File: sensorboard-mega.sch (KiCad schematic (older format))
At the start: 19 parts, among them P1 Digital, P10 CONN_01X01, P11 CONN_01X01, P12 CONN_01X01, P13 CONN_01X01, P2 Power, P3 Analog, P4 Analog, P5 PWM, P6 PWM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

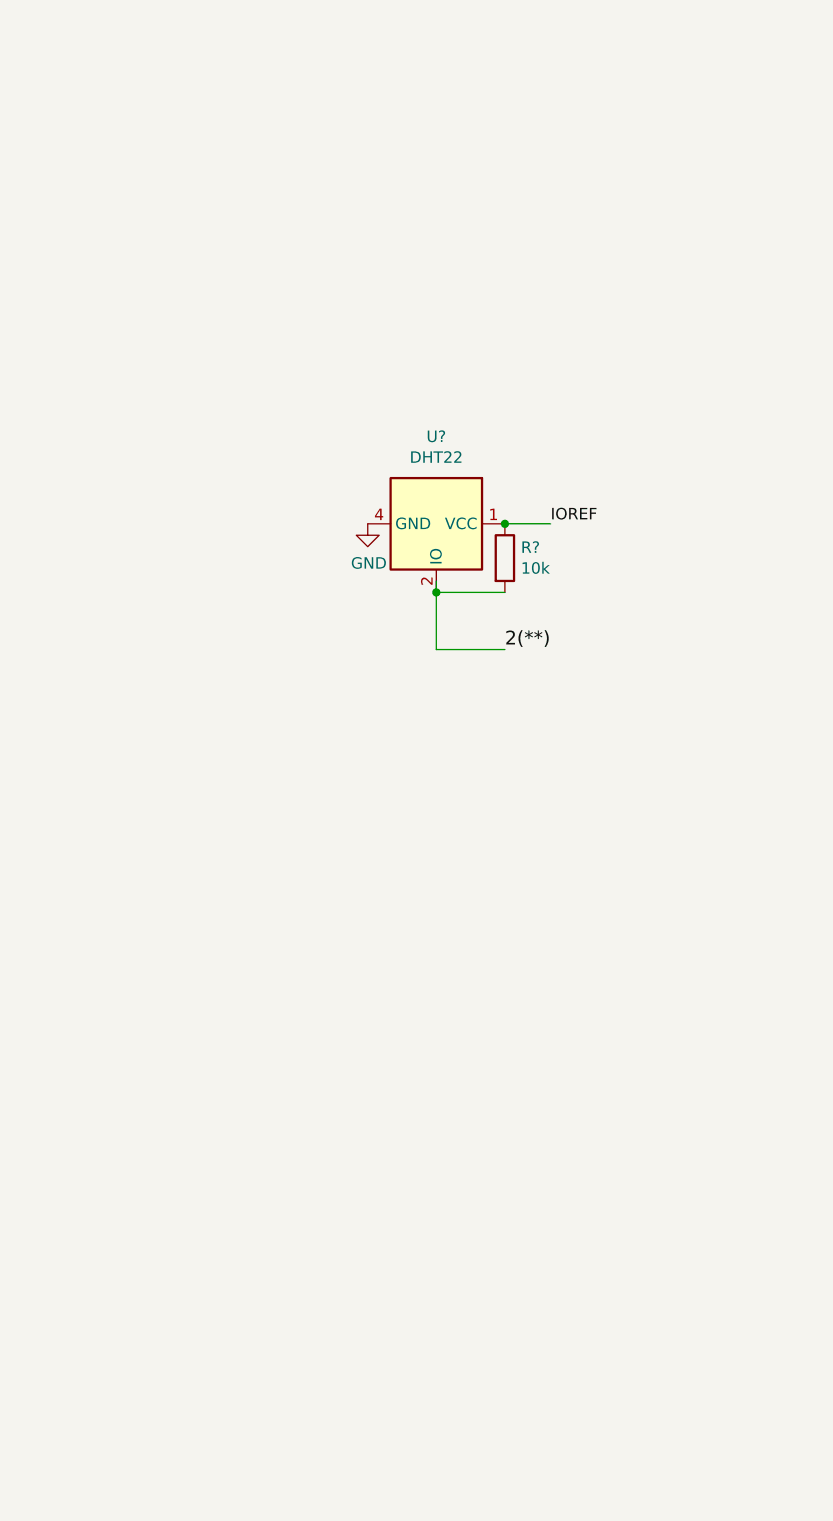
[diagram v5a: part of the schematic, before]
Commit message: Add all onboard sensors
The sensors are:
Barometer sensor
DHT22 sensor
DS3231 RTC
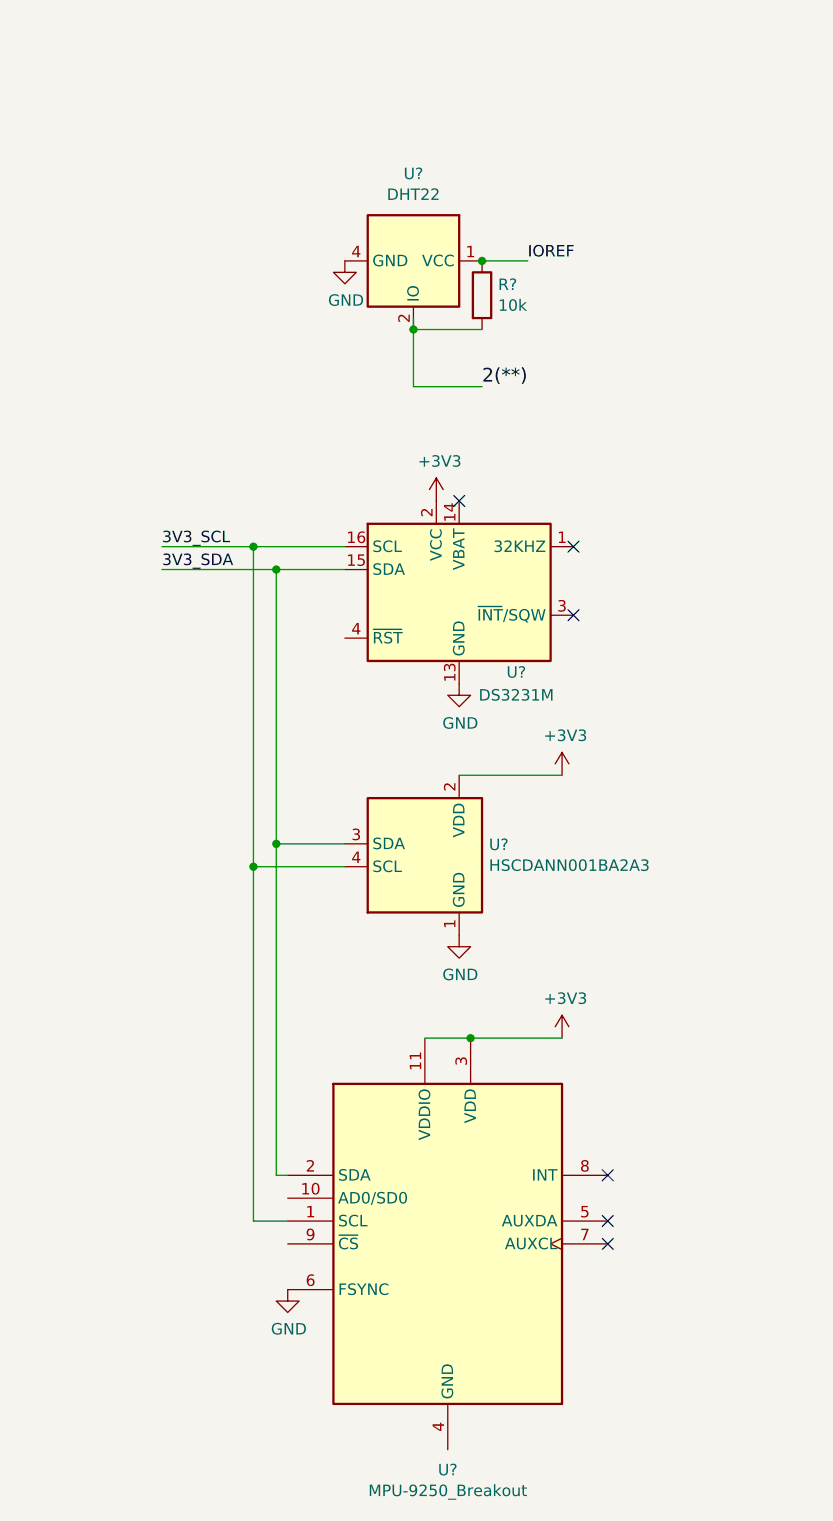
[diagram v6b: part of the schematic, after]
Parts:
- added U?: DS3231M, Package_SO:SOIC-16W_7.5x10.3mm_P1.27mm, symbol Timer_RTC:DS3231M
- added U?: HSCDANN001BA2A3, Package_DIP:DIP-8_W7.62mm, symbol New_Library:HSCDANN001BA2A3
- added U?: MPU-9250_Breakout, Sensor_Motion:InvenSense_QFN-24_3x3mm_P0.4mm, symbol New_Library:MPU-9250_Breakout
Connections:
- net +3V3: now also U?.11 (VDDIO), U?.2 (VCC), U?.2 (VDD), U?.3 (VDD)
- net 3V3_SCL: now also U?.1 (SCL), U?.16 (SCL), U?.4 (SCL)
- net 3V3_SDA: now also U?.15 (SDA), U?.2 (SDA), U?.3 (SDA)
- net GND: now also U?.1 (GND), U?.10 (GND), U?.11 (GND), U?.12 (GND), U?.13 (GND), U?.5 (GND), U?.6 (FSYNC), U?.6 (GND), U?.7 (GND), U?.8 (GND), U?.9 (GND)
- no-connect marks 7 -> 13
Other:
- moved on the sheet: R?, U?
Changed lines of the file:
@@
 $EndComp
 Wire Wire Line
-	5850 3050 6050 3050
-Text Label 6050 3050 0    50   ~ 0
+	5750 1900 5950 1900
+Text Label 5950 1900 0    50   ~ 0
 IOREF
 $Comp
 L Device:R R?
 U 1 1 5DF91E75
-P 5850 3200
-F 0 "R?" H 5920 3246 50  0000 L CNN
-F 1 "10k" H 5920 3155 50  0000 L CNN
-F 2 "" V 5780 3200 50  0001 C CNN
-F 3 "~" H 5850 3200 50  0001 C CNN
-	1    5850 3200
-	1    0    0    -1
-$EndComp
-Wire Wire Line
-	5850 3350 5550 3350
+P 5750 2050
+F 0 "R?" H 5820 2096 50  0000 L CNN
+F 1 "10k" H 5820 2005 50  0000 L CNN
+F 2 "" V 5680 2050 50  0001 C CNN
+F 3 "~" H 5750 2050 50  0001 C CNN
+	1    5750 2050
+	1    0    0    -1
+$EndComp
+Wire Wire Line
+	5750 2200 5450 2200
 $Comp
 L power:GND #PWR?
 U 1 1 5DF988E0
-P 5250 3050
-F 0 "#PWR?" H 5250 2800 50  0001 C CNN
-F 1 "GND" H 5255 2877 50  0000 C CNN
-F 2 "" H 5250 3050 50  0001 C CNN
-F 3 "" H 5250 3050 50  0001 C CNN
-	1    5250 3050
+P 5150 1900
+F 0 "#PWR?" H 5150 1650 50  0001 C CNN
+F 1 "GND" H 5155 1727 50  0000 C CNN
+F 2 "" H 5150 1900 50  0001 C CNN
+F 3 "" H 5150 1900 50  0001 C CNN
+	1    5150 1900
 	1    0    0    -1
 $EndComp
@@
 L Sensor:DHT22 U?
 U 1 1 5DF9B2BC
-P 5550 3050
-F 0 "U?" V 5169 3050 50  0000 C CNN
-F 1 "DHT22" V 5260 3050 50  0000 C CNN
-F 2 "Sensor:Aosong_DHT11_5.5x12.0_P2.54mm" H 5550 2650 50  0001 C CNN
-F 3 "http://akizukidenshi.com/download/ds/aosong/DHT11.pdf" H 5700 3300 50  0001 C CNN
-	1    5550 3050
+P 5450 1900
+F 0 "U?" V 5069 1900 50  0000 C CNN
+F 1 "DHT22" V 5160 1900 50  0000 C CNN
+F 2 "Sensor:Aosong_DHT11_5.5x12.0_P2.54mm" H 5450 1500 50  0001 C CNN
+F 3 "http://akizukidenshi.com/download/ds/aosong/DHT11.pdf" H 5600 2150 50  0001 C CNN
+	1    5450 1900
 	0    1    1    0
 $EndComp
-Connection ~ 5850 3050
+Connection ~ 5750 1900
 Text Notes 700  5500 0    50   ~ 0
 Note: Bridge the HV and LV signal pins using wire for Arduino Due
 Wire Wire Line
-	5550 3300 5550 3350
-Connection ~ 5550 3350
-Wire Wire Line
-	5550 3350 5550 3600
-Wire Wire Line
-	5550 3600 5850 3600
-Text Label 5850 3600 0    60   ~ 0
+	5450 2150 5450 2200
+Connection ~ 5450 2200
+Wire Wire Line
+	5450 2200 5450 2450
+Wire Wire Line
+	5450 2450 5750 2450
+Text Label 5750 2450 0    60   ~ 0
 2(**)
 $Comp
@@
 Text Label 800  6500 0    50   ~ 0
 3v3_SS
+$Comp
+L Timer_RTC:DS3231M U?
+U 1 1 5DEAA5E1
+P 5650 3350
+F 0 "U?" H 5900 3000 50  0000 C CNN
+F 1 "DS3231M" H 5900 2900 50  0000 C CNN
+F 2 "Package_SO:SOIC-16W_7.5x10.3mm_P1.27mm" H 5650 2750 50  0001 C CNN
+F 3 "http://datasheets.maximintegrated.com/en/ds/DS3231.pdf" H 5920 3400 50  0001 C CNN
+	1    5650 3350
+	1    0    0    -1
+$EndComp
+$Comp
+L New_Library:HSCDANN001BA2A3 U?
+U 1 1 5DEAAED6
+P 5550 4550
+F 0 "U?" H 5780 4646 50  0000 L CNN
+F 1 "HSCDANN001BA2A3" H 5780 4555 50  0000 L CNN
+F 2 "Package_DIP:DIP-8_W7.62mm" H 5550 3850 50  0001 C CNN
+F 3 "https://sensing.honeywell.com/honeywell-sensing-trustability-hsc-series-high-accurboard-mount-pressure-sensors-50099148-a-en.pdf" H 5550 4550 50  0001 C CNN
+	1    5550 4550
+	1    0    0    -1
+$EndComp
+$Comp
+L New_Library:MPU-9250_Breakout U?
+U 1 1 5DEAC0F0
+P 5600 6200
+F 0 "U?" H 5600 5211 50  0000 C CNN
+F 1 "MPU-9250_Breakout" H 5600 5120 50  0000 C CNN
+F 2 "Sensor_Motion:InvenSense_QFN-24_3x3mm_P0.4mm" H 5600 5200 50  0001 C CNN
+F 3 "https://store.invensense.com/datasheets/invensense/MPU9250REV1.0.pdf" H 5600 6050 50  0001 C CNN
+	1    5600 6200
+	1    0    0    -1
+$EndComp
+Wire Wire Line
+	5150 3150 4750 3150
+Wire Wire Line
+	4750 3150 4750 4550
+Wire Wire Line
+	5150 4550 4750 4550
+Connection ~ 4750 4550
+Wire Wire Line
+	4850 3250 5150 3250
+Wire Wire Line
+	5150 4450 4850 4450
+Connection ~ 4850 4450
+Wire Wire Line
+	4850 4450 4850 3250
+Wire Wire Line
+	4750 3150 4350 3150
+Connection ~ 4750 3150
+Wire Wire Line
+	4850 3250 4350 3250
+Connection ~ 4850 3250
+Text Label 4350 3250 0    50   ~ 0
+3V3_SDA
+Text Label 4350 3150 0    50   ~ 0
+3V3_SCL
+NoConn ~ 5650 2950
+NoConn ~ 6150 3150
+NoConn ~ 6150 3450
+NoConn ~ 6300 6100
+NoConn ~ 6300 6200
+NoConn ~ 6300 5900
+$Comp
+L power:GND #PWR?
+U 1 1 5DF6484B
+P 4900 6400
+F 0 "#PWR?" H 4900 6150 50  0001 C CNN
+F 1 "GND" H 4905 6227 50  0000 C CNN
+F 2 "" H 4900 6400 50  0001 C CNN
+F 3 "" H 4900 6400 50  0001 C CNN
+	1    4900 6400
+	1    0    0    -1
+$EndComp
+$Comp
+L power:GND #PWR?
+U 1 1 5DF67973
+P 5650 4850
+F 0 "#PWR?" H 5650 4600 50  0001 C CNN
+F 1 "GND" H 5655 4677 50  0000 C CNN
+F 2 "" H 5650 4850 50  0001 C CNN
+F 3 "" H 5650 4850 50  0001 C CNN
+	1    5650 4850
+	1    0    0    -1
+$EndComp
+Wire Wire Line
+	4900 6100 4750 6100
+Wire Wire Line
+	4750 4550 4750 6100
+Wire Wire Line
+	4900 5900 4850 5900
+Wire Wire Line
+	4850 4450 4850 5900
+Wire Wire Line
+	5500 5300 5700 5300
+Wire Wire Line
+	5700 5300 6100 5300
+Connection ~ 5700 5300
+$Comp
+L power:+3V3 #PWR?
+U 1 1 5DFA056E
+P 6100 5300
+F 0 "#PWR?" H 6100 5150 50  0001 C CNN
+F 1 "+3V3" H 6115 5473 50  0000 C CNN
+F 2 "" H 6100 5300 50  0001 C CNN
+F 3 "" H 6100 5300 50  0001 C CNN
+	1    6100 5300
+	1    0    0    -1
+$EndComp
+Wire Wire Line
+	5650 4150 6100 4150
+$Comp
+L power:+3V3 #PWR?
+U 1 1 5DFA9209
+P 6100 4150
+F 0 "#PWR?" H 6100 4000 50  0001 C CNN
+F 1 "+3V3" H 6115 4323 50  0000 C CNN
+F 2 "" H 6100 4150 50  0001 C CNN
+F 3 "" H 6100 4150 50  0001 C CNN
+	1    6100 4150
+	1    0    0    -1
+$EndComp
+$Comp
+L power:GND #PWR?
+U 1 1 5DFAA3A6
+P 5650 3750
+F 0 "#PWR?" H 5650 3500 50  0001 C CNN
+F 1 "GND" H 5655 3577 50  0000 C CNN
+F 2 "" H 5650 3750 50  0001 C CNN
+F 3 "" H 5650 3750 50  0001 C CNN
+	1    5650 3750
+	1    0    0    -1
+$EndComp
+$Comp
+L power:+3V3 #PWR?
+U 1 1 5DFAFB69
+P 5550 2950
+F 0 "#PWR?" H 5550 2800 50  0001 C CNN
+F 1 "+3V3" H 5565 3123 50  0000 C CNN
+F 2 "" H 5550 2950 50  0001 C CNN
+F 3 "" H 5550 2950 50  0001 C CNN
+	1    5550 2950
+	1    0    0    -1
+$EndComp
 $EndSCHEMATC

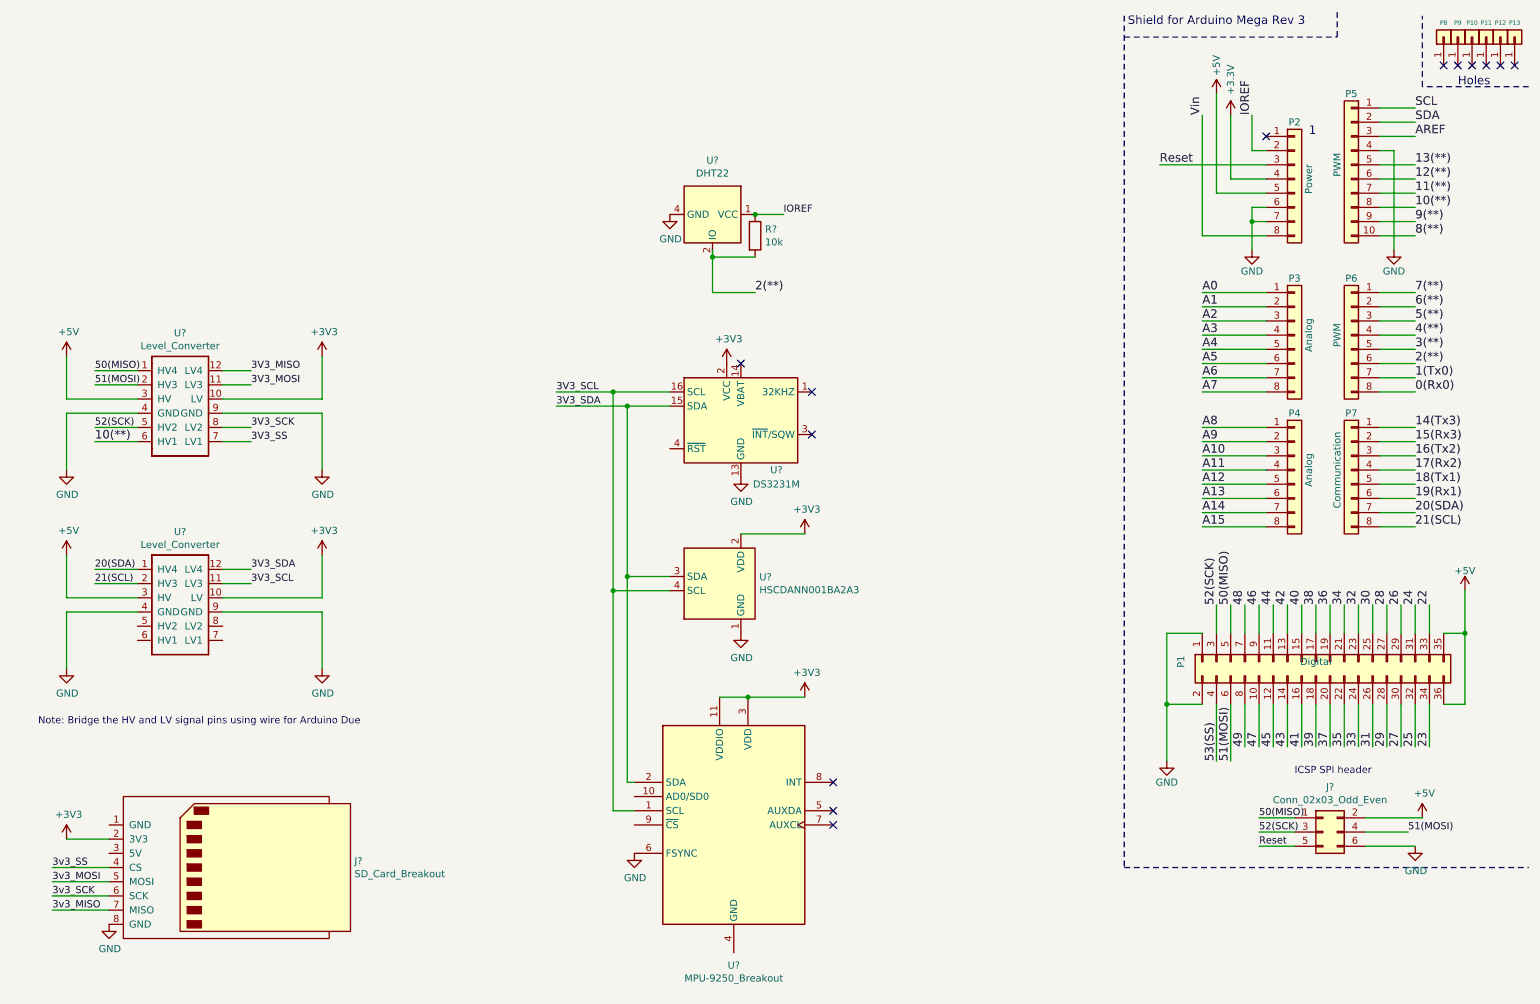
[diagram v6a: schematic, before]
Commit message: Add indicator LED array and external sensor connector
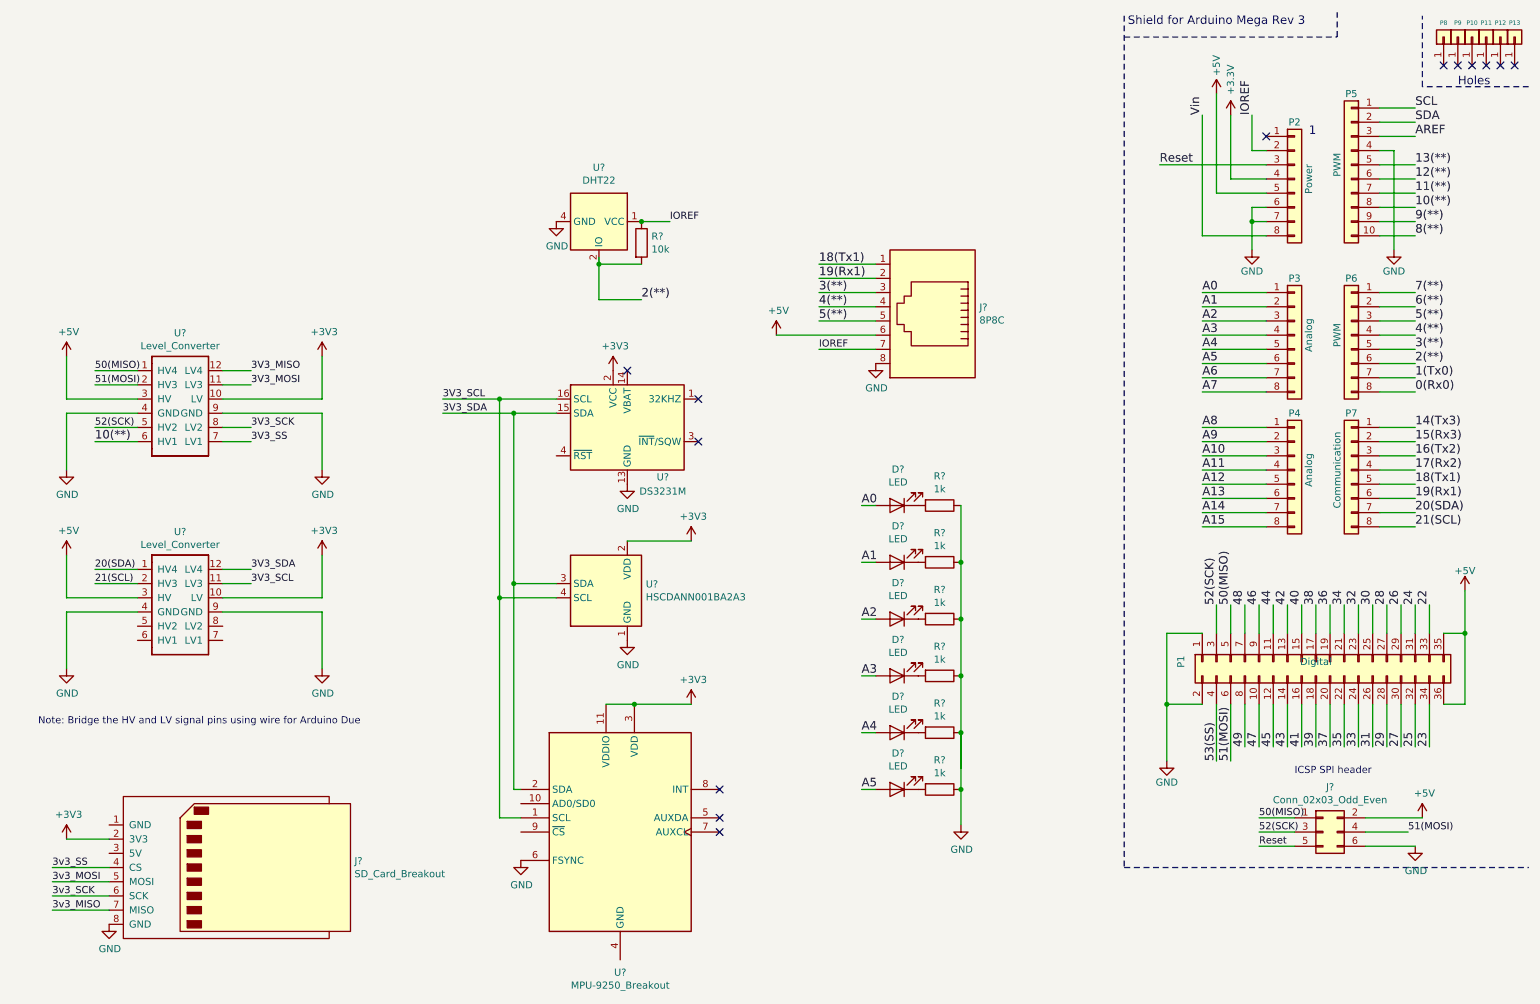
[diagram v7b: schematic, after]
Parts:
- added D? (x6): LED, symbol Device:LED
- added J?: 8P8C, symbol Connector:8P8C
- added R? (x6): 1k, symbol Device:R
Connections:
- net +5V: now also J?.6
- net 18(Tx1): now also J?.1
- net 19(Rx1): now also J?.2
- net 3(**): now also J?.3
- net 4(**): now also J?.4
- net 5(**): now also J?.5
- net A0: now also D?.2 (A)
- net A1: now also D?.2 (A)
- net A2: now also D?.2 (A)
- net A3: now also D?.2 (A)
- net A4: now also D?.2 (A)
- net A5: now also D?.2 (A)
- net GND: now also J?.8, R?.1, R?.1, R?.1, R?.1, R?.1, R?.1
- net IOREF: now also J?.7
- new net: D?.1 (K), R?.2 (x6)
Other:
- moved on the sheet: R?, U?

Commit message: Add more sensors
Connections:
- net GND: now also J?.1 (GND)
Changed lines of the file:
@@
 Wire Wire Line
 	7200 5950 7200 6200
+Wire Wire Line
+	1200 6200 1200 5750
+Wire Wire Line
+	1200 5750 600  5750
+$Comp
+L power:GND #PWR?
+U 1 1 5E131F4E
+P 600 5750
+F 0 "#PWR?" H 600 5500 50  0001 C CNN
+F 1 "GND" H 605 5577 50  0000 C CNN
+F 2 "" H 600 5750 50  0001 C CNN
+F 3 "" H 600 5750 50  0001 C CNN
+	1    600  5750
+	1    0    0    -1
+$EndComp
 $EndSCHEMATC
